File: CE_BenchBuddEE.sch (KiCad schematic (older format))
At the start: 0 parts

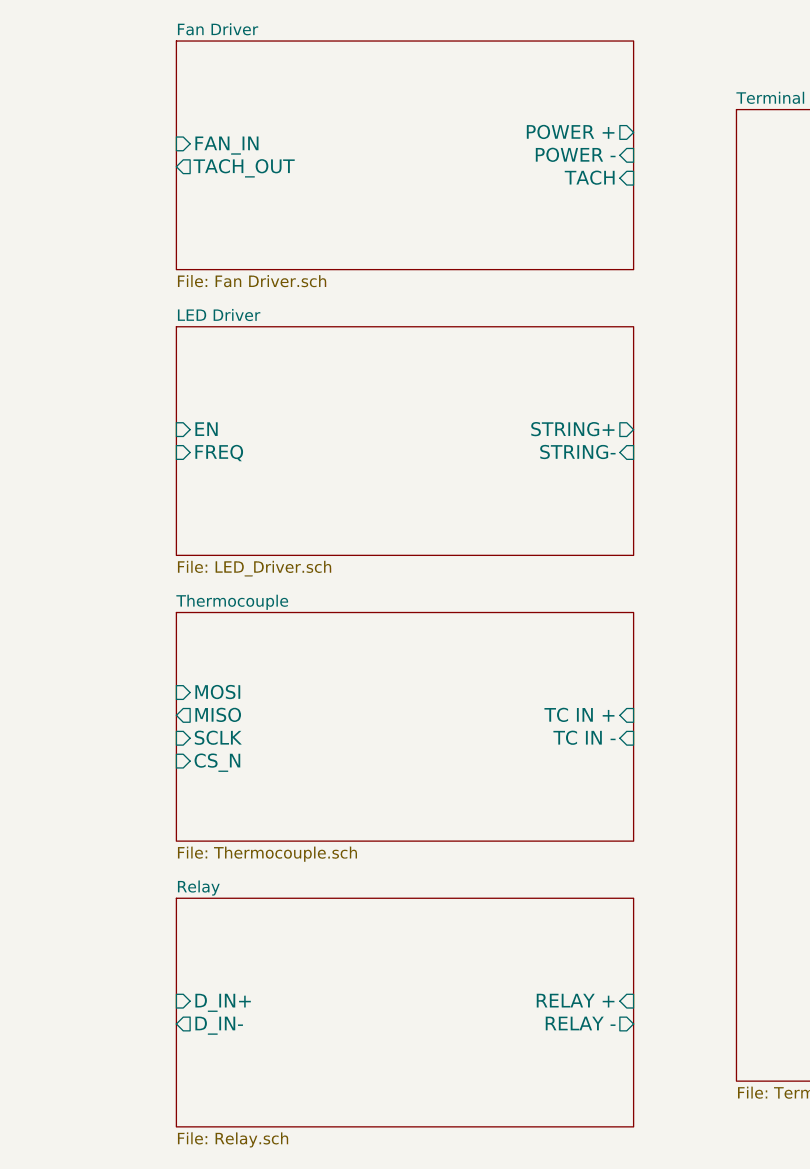
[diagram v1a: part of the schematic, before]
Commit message: Added Relay and Fan subsystem block diagrams
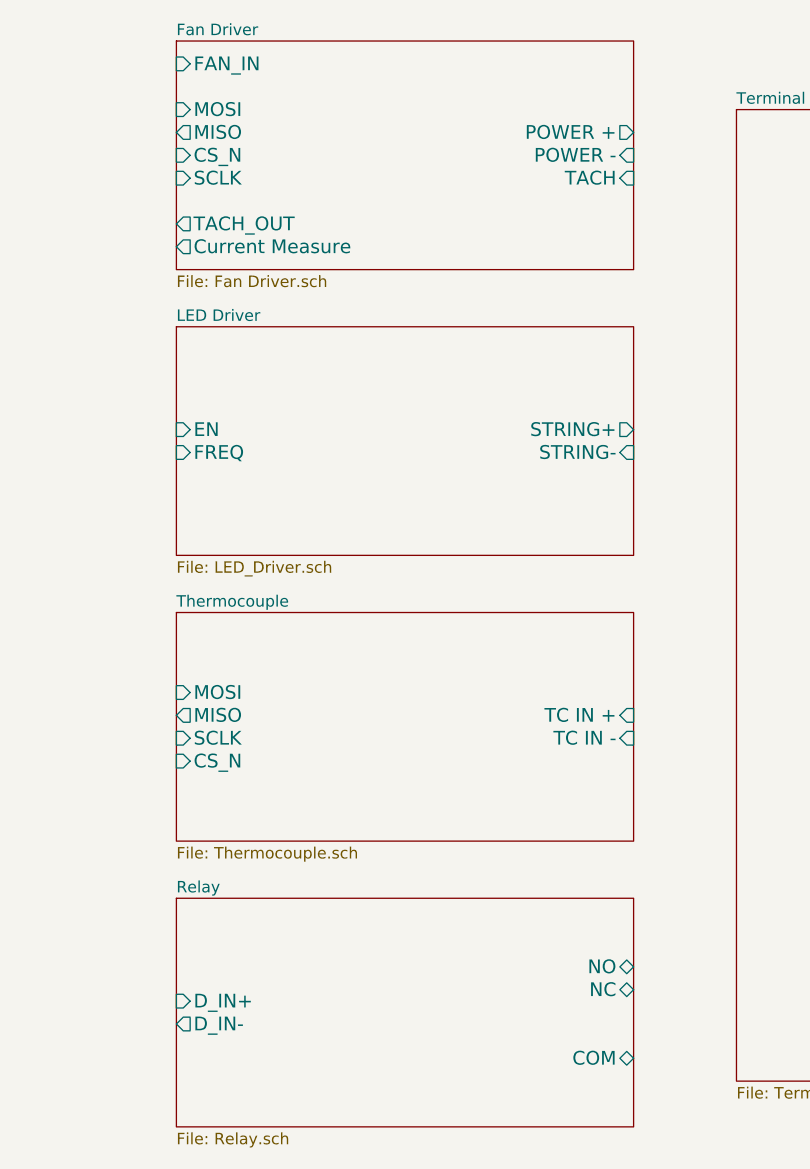
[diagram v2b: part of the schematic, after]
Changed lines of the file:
@@
 LIBS:contrib
 LIBS:valves
+LIBS:CE_BenchBuddEE
 LIBS:CE_BenchBuddEE-cache
 EELAYER 27 0
@@
 Sheet 1 8
 Title ""
-Date "4 feb 2014"
+Date "5 feb 2014"
 Rev ""
 Comp ""
@@
 F3 "POWER -" I R 8600 1950 60
 F4 "TACH" I R 8600 2050 60
-F5 "TACH_OUT" O L 6600 2000 60
-F6 "FAN_IN" I L 6600 1900 60
+F5 "TACH_OUT" O L 6600 2250 60
+F6 "FAN_IN" I L 6600 1550 60
+F7 "Current Measure" O L 6600 2350 60
+F8 "MOSI" I L 6600 1750 60
+F9 "MISO" O L 6600 1850 60
+F10 "CS_N" I L 6600 1950 60
+F11 "SCLK" I L 6600 2050 60
 $EndSheet
 $Sheet
@@
 F2 "D_IN+" I L 6600 5650 60
 F3 "D_IN-" O L 6600 5750 60
-F4 "RELAY +" I R 8600 5650 60
-F5 "RELAY -" O R 8600 5750 60
+F4 "NC" B R 8600 5600 60
+F5 "NO" B R 8600 5500 60
+F6 "COM" B R 8600 5900 60
 $EndSheet
 $Sheet

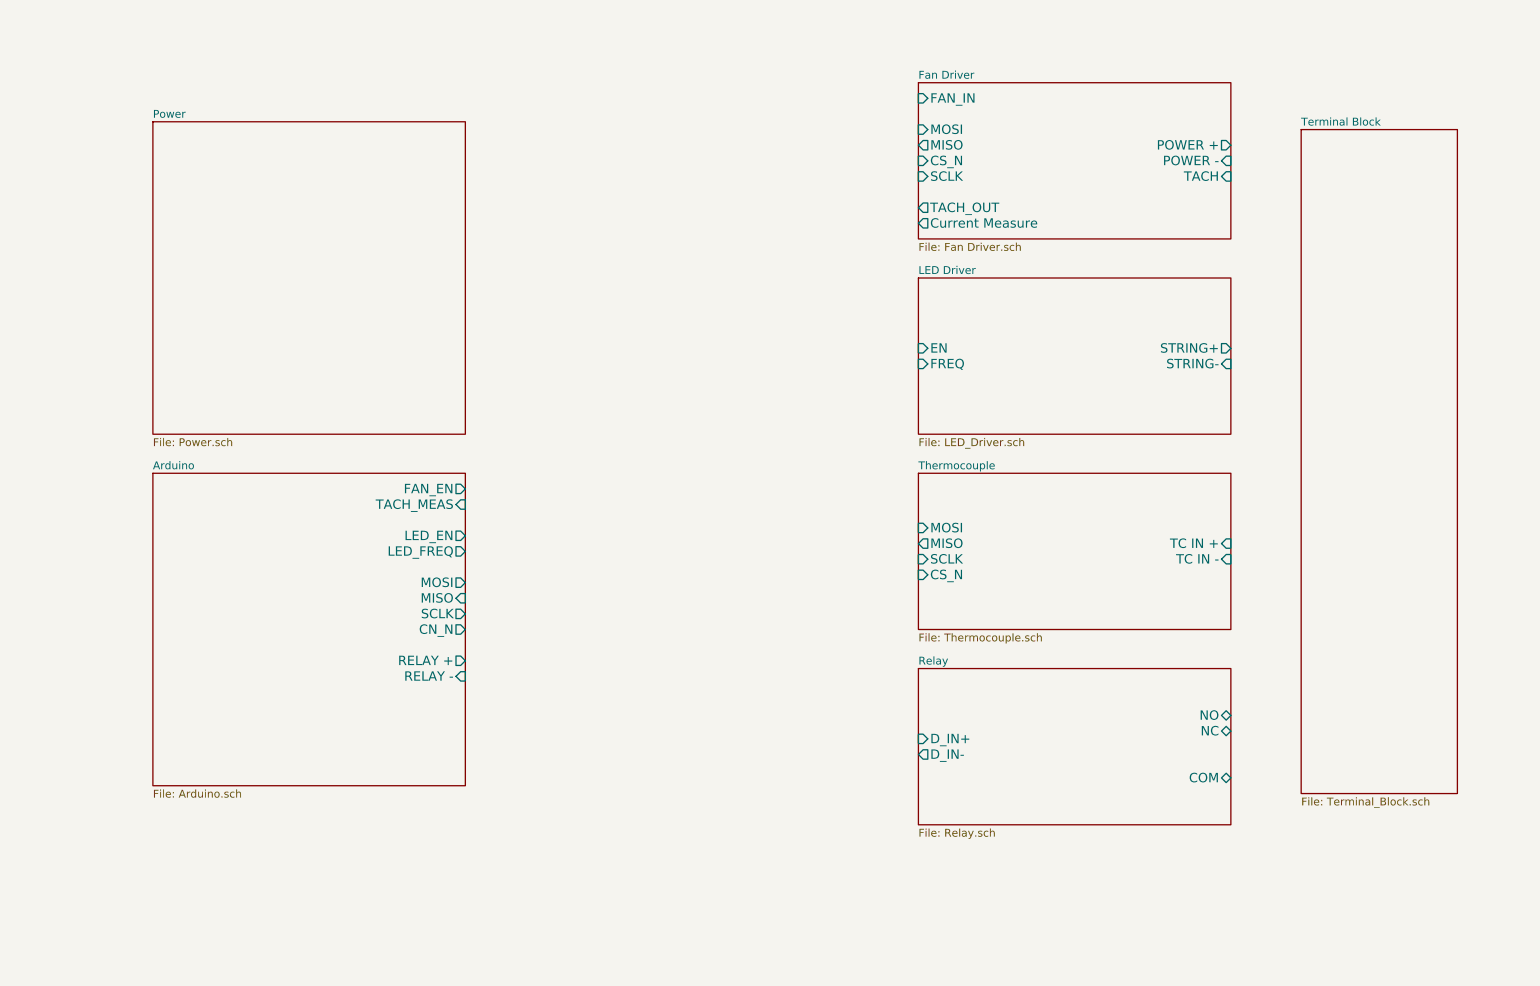
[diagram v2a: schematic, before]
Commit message: Blocked out the LED Driver and Power sheets
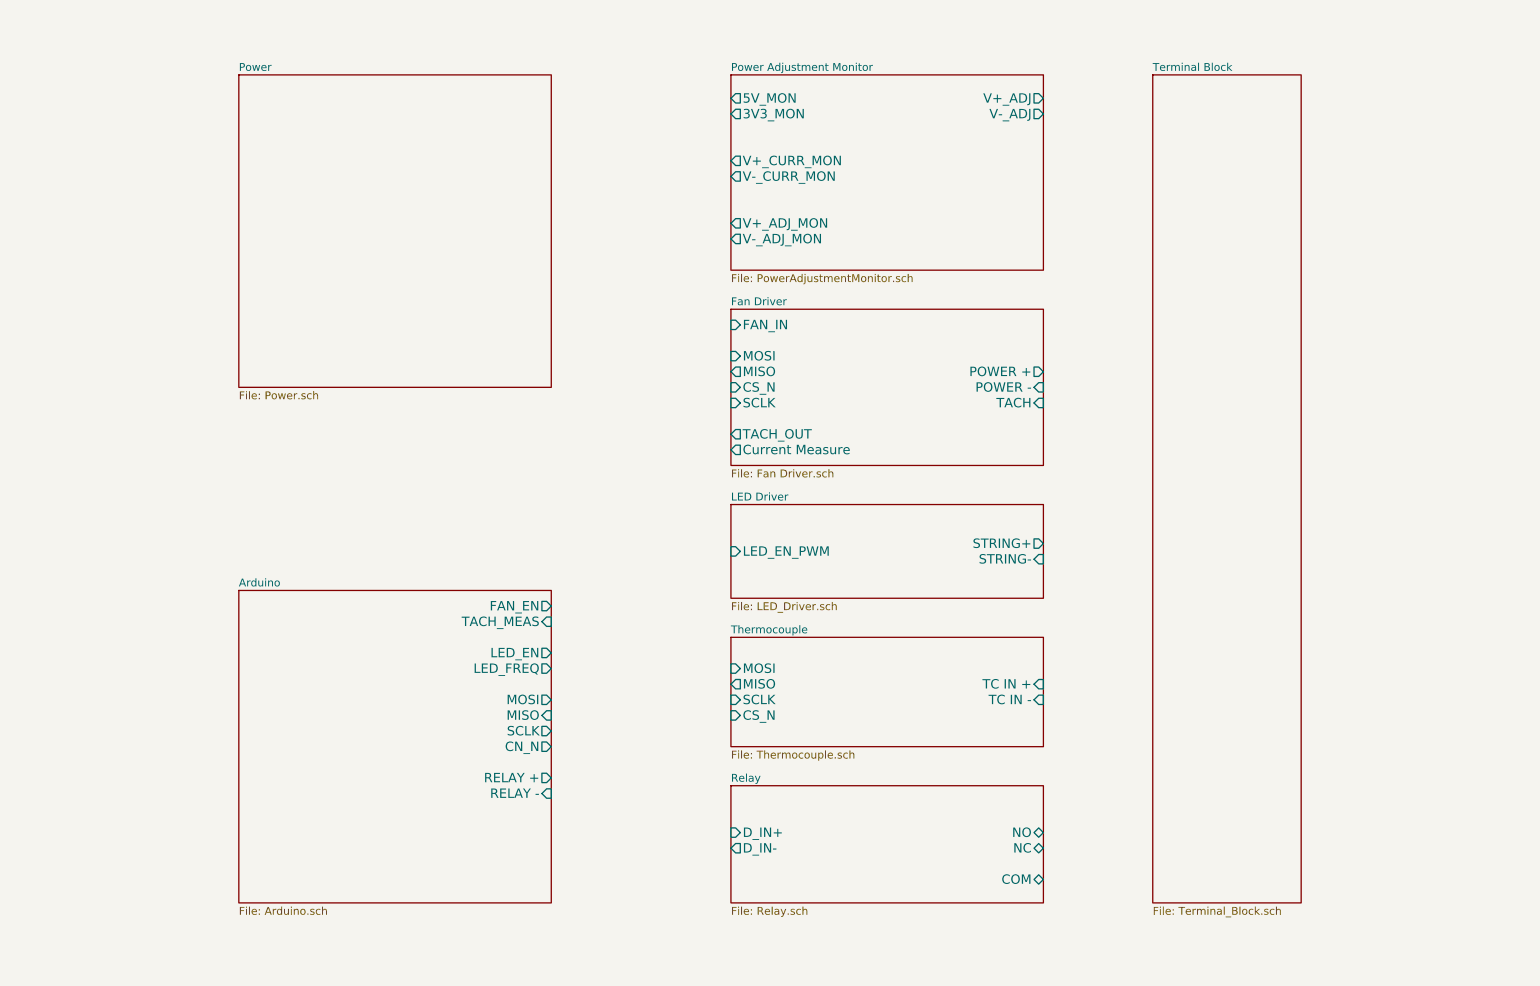
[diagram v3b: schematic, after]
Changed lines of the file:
@@
 LIBS:contrib
 LIBS:valves
+LIBS:CE_BenchBuddEE-cache
 LIBS:CE_BenchBuddEE
 LIBS:CE_BenchBuddEE-cache
@@
 $Descr A4 11693 8268
 encoding utf-8
-Sheet 1 8
+Sheet 1 9
 Title ""
-Date "5 feb 2014"
+Date "6 feb 2014"
 Rev ""
 Comp ""
@@
 $EndDescr
 $Sheet
-S 1700 1700 2000 2000
+S 5400 2900 2000 1000
+U 52EBF362
+F0 "Fan Driver" 50
+F1 "Fan Driver.sch" 50
+F2 "POWER +" O R 7400 3300 60
+F3 "POWER -" I R 7400 3400 60
+F4 "TACH" I R 7400 3500 60
+F5 "TACH_OUT" O L 5400 3700 60
+F6 "FAN_IN" I L 5400 3000 60
+F7 "Current Measure" O L 5400 3800 60
+F8 "MOSI" I L 5400 3200 60
+F9 "MISO" O L 5400 3300 60
+F10 "CS_N" I L 5400 3400 60
+F11 "SCLK" I L 5400 3500 60
+$EndSheet
+$Sheet
+S 5400 5000 2000 700
+U 52EBF2F6
+F0 "Thermocouple" 50
+F1 "Thermocouple.sch" 50
+F2 "TC IN +" I R 7400 5300 60
+F3 "TC IN -" I R 7400 5400 60
+F4 "MOSI" I L 5400 5200 60
+F5 "MISO" O L 5400 5300 60
+F6 "SCLK" I L 5400 5400 60
+F7 "CS_N" I L 5400 5500 60
+$EndSheet
+$Sheet
+S 5400 5950 2000 750
+U 52EBF302
+F0 "Relay" 50
+F1 "Relay.sch" 50
+F2 "D_IN+" I L 5400 6250 60
+F3 "D_IN-" O L 5400 6350 60
+F4 "NC" B R 7400 6350 60
+F5 "NO" B R 7400 6250 60
+F6 "COM" B R 7400 6550 60
+$EndSheet
+$Sheet
+S 2250 4700 2000 2000
+U 52EBF29E
+F0 "Arduino" 50
+F1 "Arduino.sch" 50
+F2 "RELAY +" O R 4250 5900 60
+F3 "RELAY -" I R 4250 6000 60
+F4 "MOSI" O R 4250 5400 60
+F5 "MISO" I R 4250 5500 60
+F6 "SCLK" O R 4250 5600 60
+F7 "CN_N" O R 4250 5700 60
+F8 "LED_EN" O R 4250 5100 60
+F9 "LED_FREQ" O R 4250 5200 60
+F10 "FAN_EN" O R 4250 4800 60
+F11 "TACH_MEAS" I R 4250 4900 60
+$EndSheet
+$Sheet
+S 8100 1400 950  5300
+U 52EBF38D
+F0 "Terminal Block" 50
+F1 "Terminal_Block.sch" 50
+$EndSheet
+$Sheet
+S 2250 1400 2000 2000
 U 52EBF30F
 F0 "Power" 50
@@
 $EndSheet
 $Sheet
-S 6600 2700 2000 1000
+S 5400 4150 2000 600
 U 52EBF33E
 F0 "LED Driver" 50
 F1 "LED_Driver.sch" 50
-F2 "EN" I L 6600 3150 60
-F3 "FREQ" I L 6600 3250 60
-F4 "STRING+" O R 8600 3150 60
-F5 "STRING-" I R 8600 3250 60
+F2 "STRING+" O R 7400 4400 60
+F3 "STRING-" I R 7400 4500 60
+F4 "LED_EN_PWM" I L 5400 4450 60
 $EndSheet
 $Sheet
-S 6600 1450 2000 1000
-U 52EBF362
-F0 "Fan Driver" 50
-F1 "Fan Driver.sch" 50
-F2 "POWER +" O R 8600 1850 60
-F3 "POWER -" I R 8600 1950 60
-F4 "TACH" I R 8600 2050 60
-F5 "TACH_OUT" O L 6600 2250 60
-F6 "FAN_IN" I L 6600 1550 60
-F7 "Current Measure" O L 6600 2350 60
-F8 "MOSI" I L 6600 1750 60
-F9 "MISO" O L 6600 1850 60
-F10 "CS_N" I L 6600 1950 60
-F11 "SCLK" I L 6600 2050 60
-$EndSheet
-$Sheet
-S 6600 3950 2000 1000
-U 52EBF2F6
-F0 "Thermocouple" 50
-F1 "Thermocouple.sch" 50
-F2 "TC IN +" I R 8600 4400 60
-F3 "TC IN -" I R 8600 4500 60
-F4 "MOSI" I L 6600 4300 60
-F5 "MISO" O L 6600 4400 60
-F6 "SCLK" I L 6600 4500 60
-F7 "CS_N" I L 6600 4600 60
-$EndSheet
-$Sheet
-S 6600 5200 2000 1000
-U 52EBF302
-F0 "Relay" 50
-F1 "Relay.sch" 50
-F2 "D_IN+" I L 6600 5650 60
-F3 "D_IN-" O L 6600 5750 60
-F4 "NC" B R 8600 5600 60
-F5 "NO" B R 8600 5500 60
-F6 "COM" B R 8600 5900 60
-$EndSheet
-$Sheet
-S 1700 3950 2000 2000
-U 52EBF29E
-F0 "Arduino" 50
-F1 "Arduino.sch" 50
-F2 "RELAY +" O R 3700 5150 60
-F3 "RELAY -" I R 3700 5250 60
-F4 "MOSI" O R 3700 4650 60
-F5 "MISO" I R 3700 4750 60
-F6 "SCLK" O R 3700 4850 60
-F7 "CN_N" O R 3700 4950 60
-F8 "LED_EN" O R 3700 4350 60
-F9 "LED_FREQ" O R 3700 4450 60
-F10 "FAN_EN" O R 3700 4050 60
-F11 "TACH_MEAS" I R 3700 4150 60
-$EndSheet
-$Sheet
-S 9050 1750 1000 4250
-U 52EBF38D
-F0 "Terminal Block" 50
-F1 "Terminal_Block.sch" 50
+S 5400 1400 2000 1250
+U 52F2E147
+F0 "Power Adjustment Monitor" 50
+F1 "PowerAdjustmentMonitor.sch" 50
+F2 "V+_ADJ" O R 7400 1550 60
+F3 "V-_ADJ" O R 7400 1650 60
+F4 "3V3_MON" O L 5400 1650 60
+F5 "5V_MON" O L 5400 1550 60
+F6 "V+_ADJ_MON" O L 5400 2350 60
+F7 "V-_ADJ_MON" O L 5400 2450 60
+F8 "V+_CURR_MON" O L 5400 1950 60
+F9 "V-_CURR_MON" O L 5400 2050 60
 $EndSheet
 $EndSCHEMATC
